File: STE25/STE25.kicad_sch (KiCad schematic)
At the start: 250 parts, among them P202 LAUTSTAERKE, P203 R_Potentiometer, Q201 16.0, Q202 3.686, SW201 RESET, T201 BC547, T204 BC547, T205 BC547, T206 BC547, T207 BD679, T208 BD679, T209 BC556, T210 BC547, T211 BC547, T212 BC547

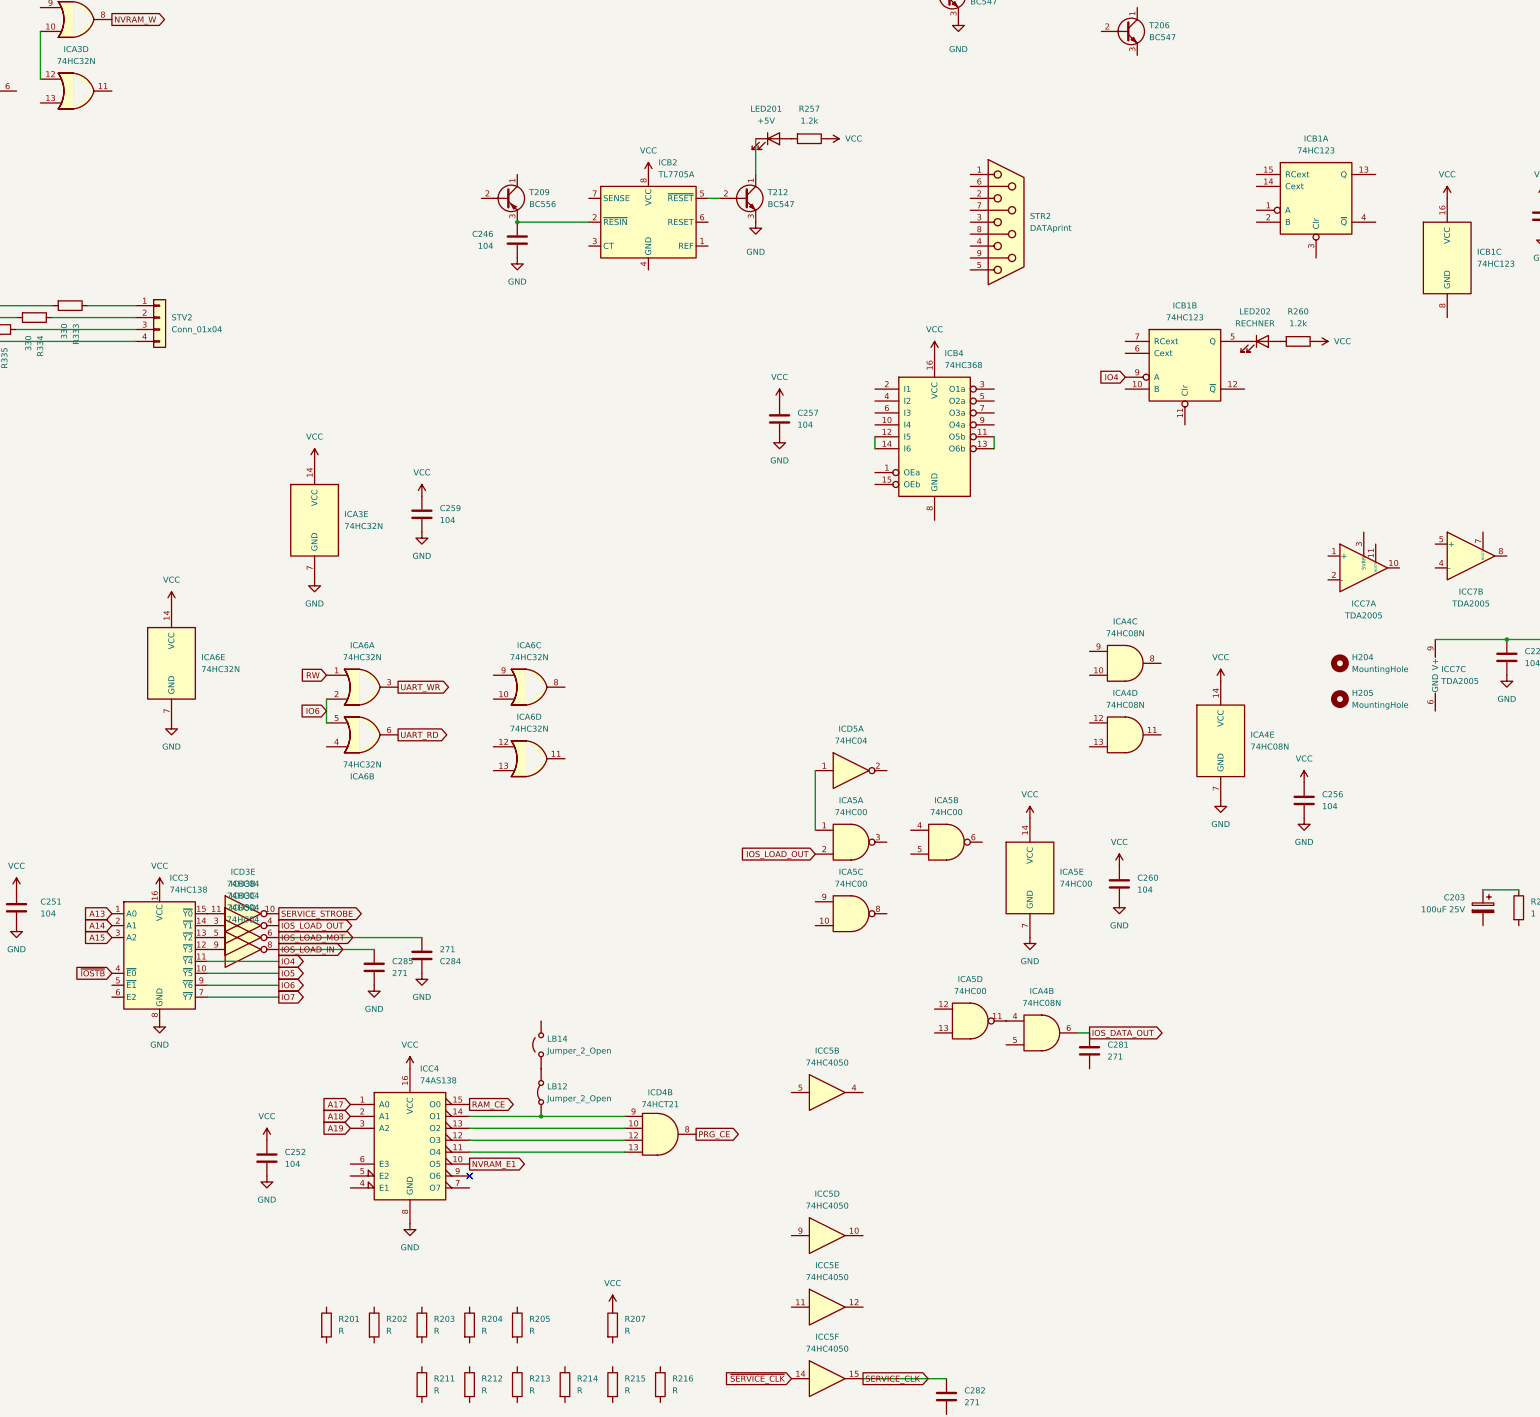
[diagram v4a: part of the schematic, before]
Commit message: onboard rom
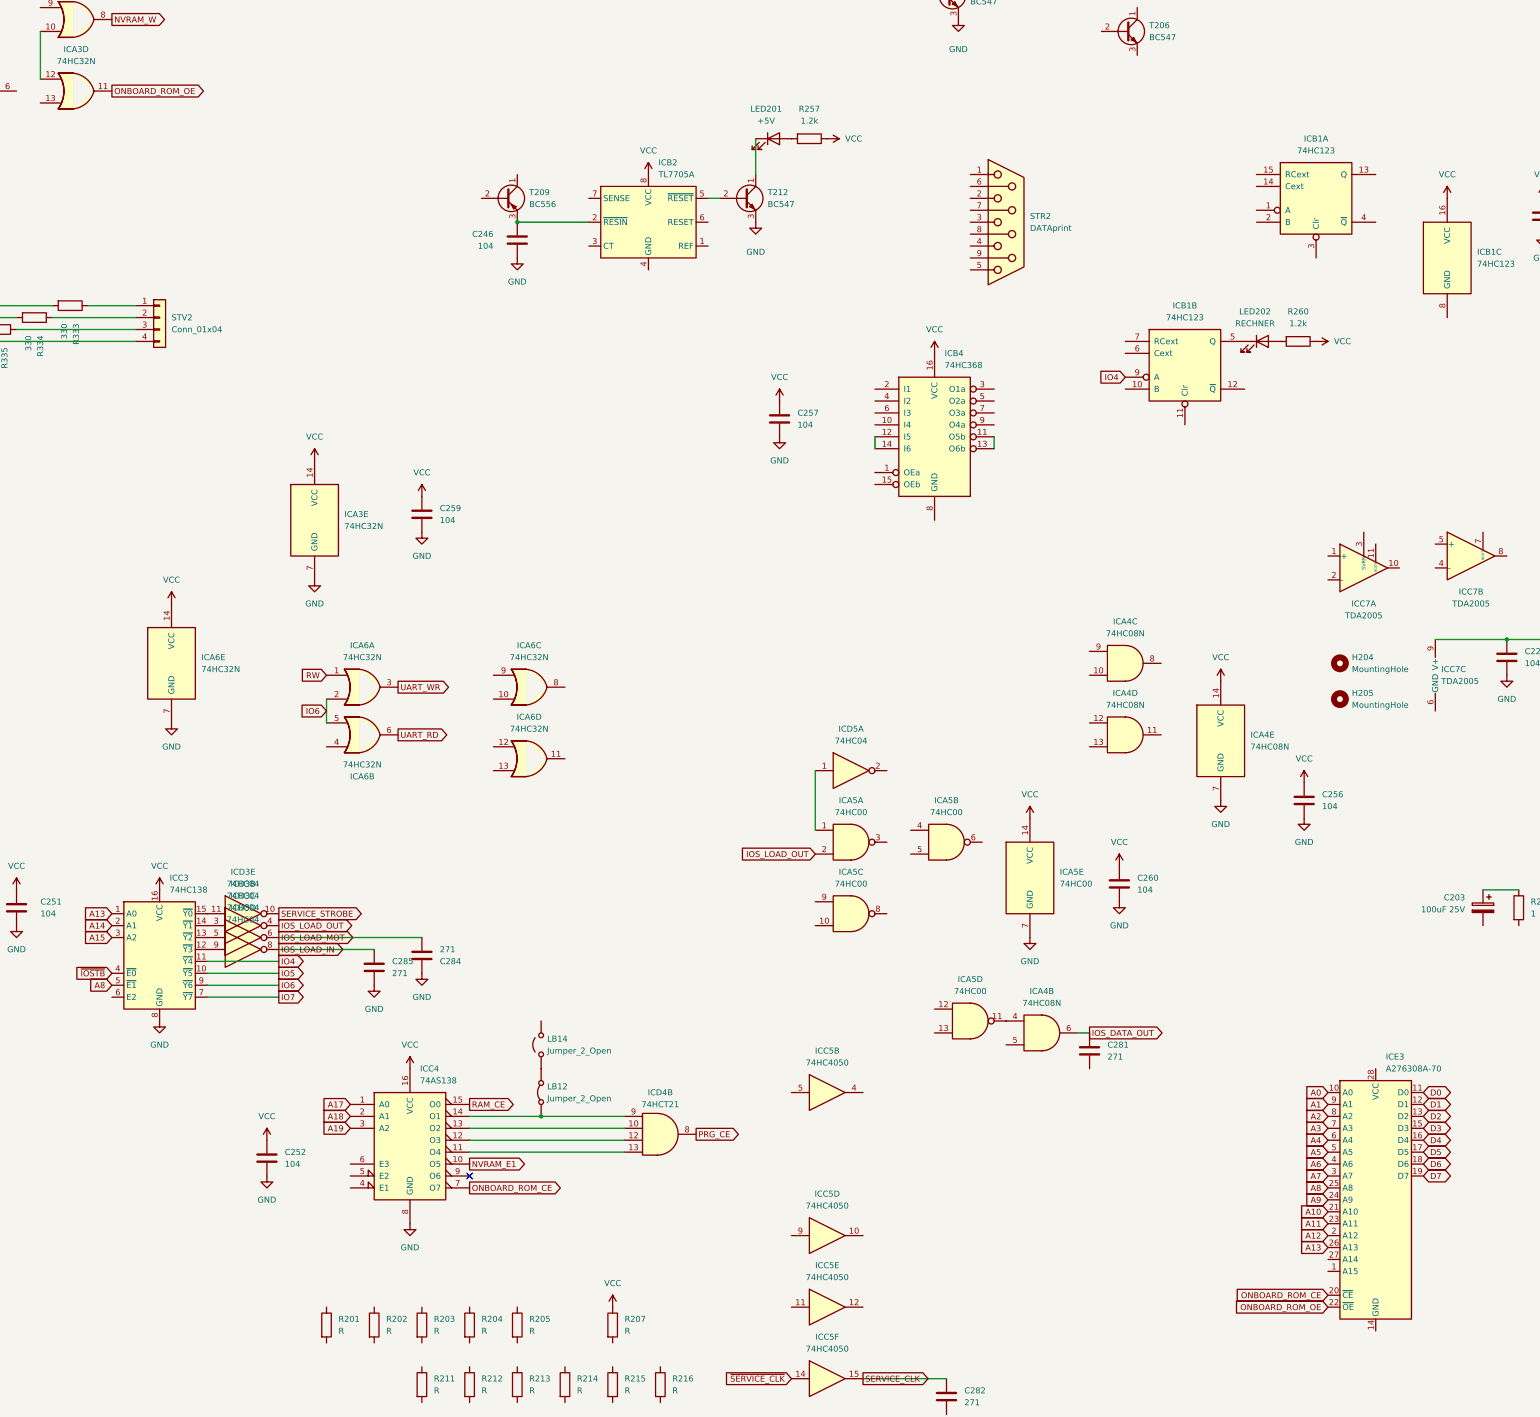
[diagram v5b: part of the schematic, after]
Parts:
- added ICE3: A276308A-70, Package_DIP:DIP-28_W15.24mm, symbol Memory_EPROM:27C512
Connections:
- net A0: now also ICE3.10 (A0)
- net A1: now also ICE3.9 (A1)
- net A10: now also ICE3.21 (A10)
- net A11: now also ICE3.23 (A11)
- net A12: now also ICE3.2 (A12)
- net A13: now also ICE3.26 (A13)
- net A2: now also ICE3.8 (A2)
- net A3: now also ICE3.7 (A3)
- net A4: now also ICE3.6 (A4)
- net A5: now also ICE3.5 (A5)
- net A6: now also ICE3.4 (A6)
- net A7: now also ICE3.3 (A7)
- net A8: now also ICC3.5 (~{E1}), ICE3.25 (A8)
- net A9: now also ICE3.24 (A9)
- net D0: now also ICE3.11 (D0)
- net D1: now also ICE3.12 (D1)
- net D2: now also ICE3.13 (D2)
- net D3: now also ICE3.15 (D3)
- net D4: now also ICE3.16 (D4)
- net D5: now also ICE3.17 (D5)
- net D6: now also ICE3.18 (D6)
- net D7: now also ICE3.19 (D7)
- net ONBOARD_ROM_OE: now reaches ICA3.11
- net ONBOARD_ROM_OE: now also ICE3.22 (~{OE})
- net ONBOARD_ROM_CE: now reaches ICC4.7 (O7)
- net ONBOARD_ROM_CE: now also ICE3.20 (~{CE})
